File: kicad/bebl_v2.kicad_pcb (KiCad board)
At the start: 2 copper layers, 80 x 44 mm, 72 parts, among them P1 ISP, P10 LED_CHG, P11 LED_1, P12 LED_2, P13 LED_3, P14 LED_PWR, P2 FTDI, P3 LED_1, P4 LED_2, P5 LED_3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

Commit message: work in progress
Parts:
- D4: value LED_B -> LED_D
- D7: value LED_D -> LED_B
- R10, R11, R12, R7, R8, R9: value 56E -> 22E
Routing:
- net /LED_brd/LEDP2: track 20.7 -> 21.5 mm
- net /LED_brd/LEDP1: track 11.2 -> 11.9 mm

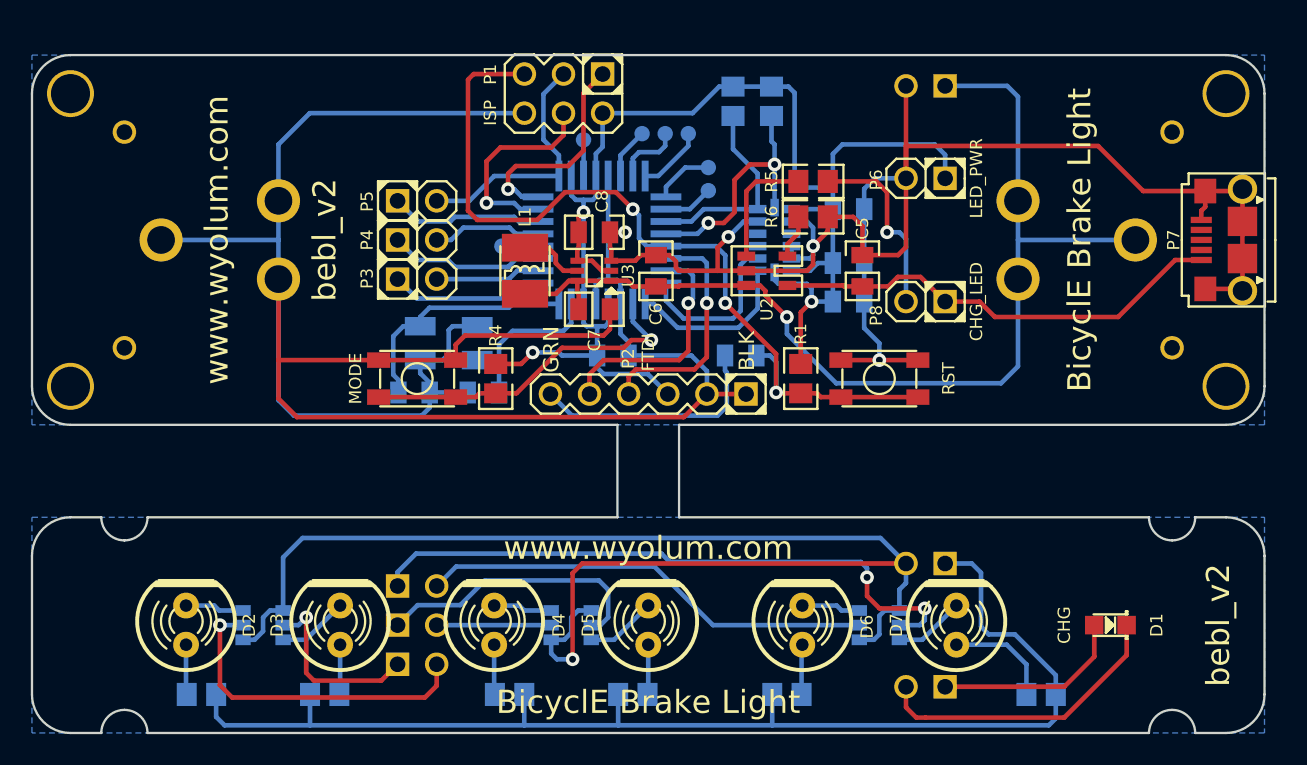
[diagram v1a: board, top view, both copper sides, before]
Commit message: made LED board smaller
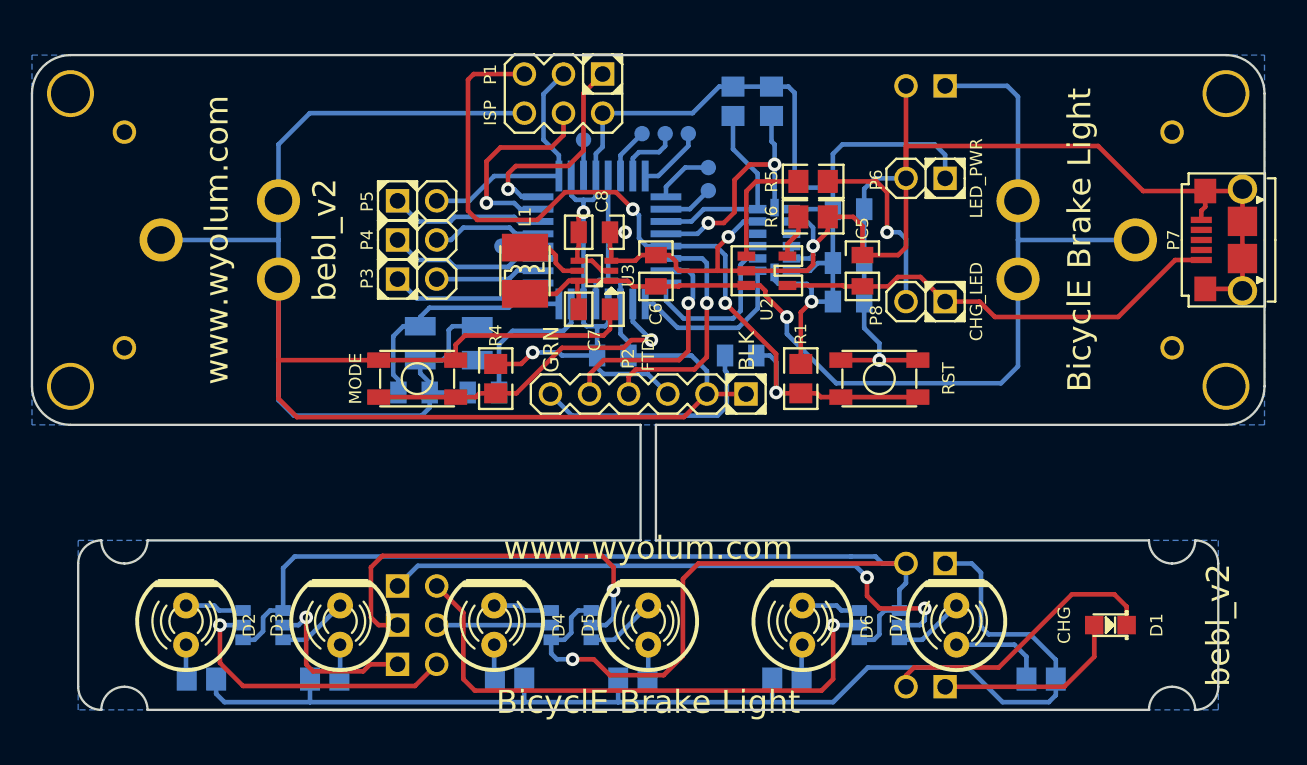
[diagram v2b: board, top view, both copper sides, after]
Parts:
- moved R10 1.00 mm to (73.0, 78.5)
- moved R11 1.00 mm to (83.0, 78.5)
- moved R12 1.00 mm to (99.5, 78.5)
- moved R7 1.00 mm to (45.0, 78.5)
- moved R8 1.00 mm to (53.0, 78.5)
- moved R9 1.00 mm to (65.0, 78.5)
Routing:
- net /LED_brd/LEDD3: track 18.2 -> 26.5 mm, vias 0 -> 1
- net /LED_brd/LEDB6: track 29.5 -> 36.6 mm, vias 0 -> 1
- net /LED_brd/LEDP2: track 21.5 -> 19.2 mm
- net /LED_brd/3V3_LED: track 79.4 -> 77.8 mm
- net /LED_brd/LEDP5: track 40.7 -> 39.2 mm
- net Net-(D6-Pad1): track 3.25 -> 2.25 mm
- net Net-(D5-Pad1): track 3.25 -> 2.25 mm
- net Net-(D4-Pad1): track 3.25 -> 2.25 mm
- net Net-(D3-Pad1): track 3.25 -> 2.25 mm
- net Net-(D2-Pad1): track 3.25 -> 2.25 mm
- net /LED_brd/GND_LED: track 90.2 -> 89.3 mm
- net /LED_brd/LEDP1: track 11.9 -> 11.1 mm
- net /LED_brd/LEDK: track 19.6 -> 18.8 mm
- net Net-(D7-Pad1): track 7.03 -> 6.32 mm
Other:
- board size 80 x 44 mm -> 80 x 42.5 mm

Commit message: bebl_v2 gerbers ready. BoM pending
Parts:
- added G***: LOGO, bebl_v2_legacy:OSHW_6mm, F.Cu at (76.5, 41.8)
- added G***: LOGO, bebl_v2_legacy:OSHW_6mm, F.Cu at (100.2, 75.0)
- added G1: Logo-WL3, bebl_v2_legacy:Logo-WL3, F.Cu at (33.8, 53.2)
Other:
- board text added: "+x"
- board text added: "+y"
- board text added: "+z"
- board text added: "OpenHardware"

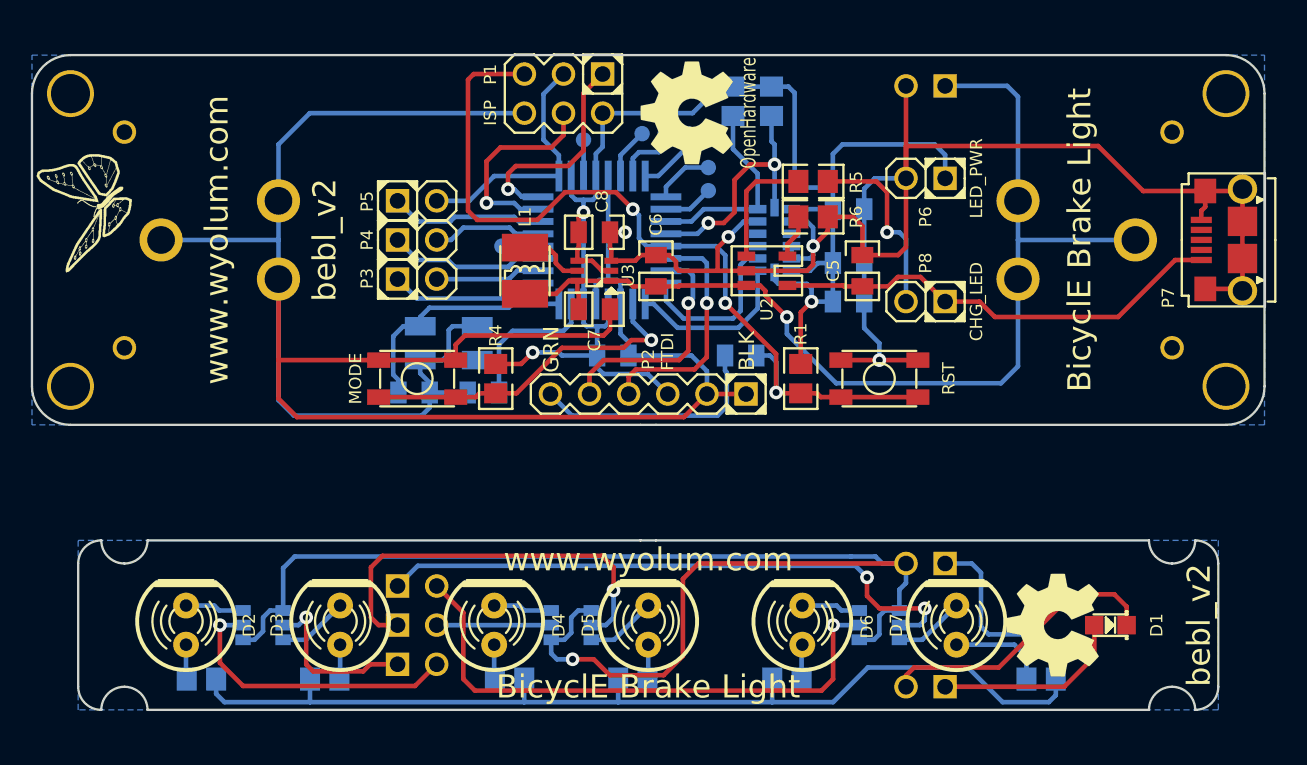
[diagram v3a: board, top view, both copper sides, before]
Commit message: footprint errors corrected, BoM ready, but pending seeed format
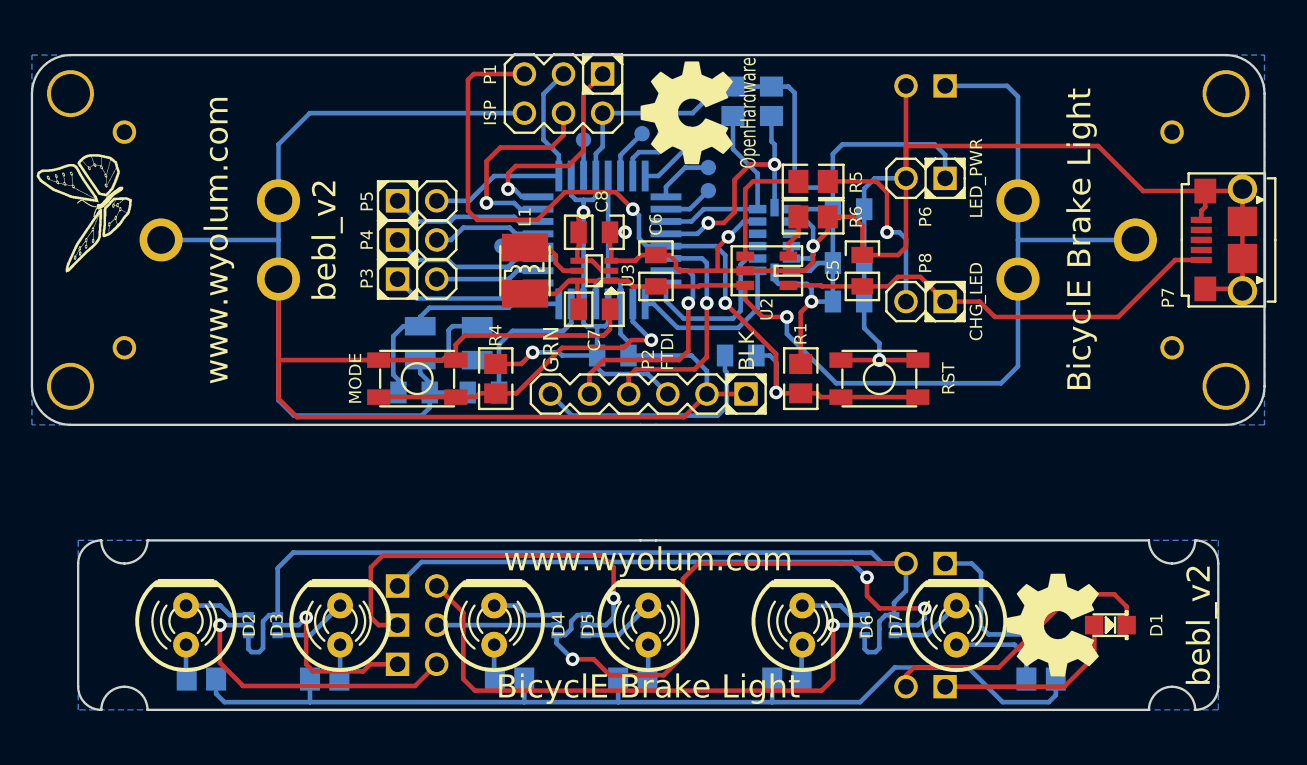
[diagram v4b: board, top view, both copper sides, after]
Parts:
- Q1, Q2, Q3: footprint bebl_v2_pretty:SOT23-6 -> bebl_v2_pretty:SOT363
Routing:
- net /LED_brd/GND_LED: track 89.3 -> 90.7 mm
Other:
- net class 0.2mm: clearance 0.2 -> 0.15
- net class Default: clearance 0.25 -> 0.15
- rule trace_clearance: 0.25 -> 0.15
